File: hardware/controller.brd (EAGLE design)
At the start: 44.5 x 33 mm, 27 parts, among them IC3 TS5205, J1 PIN2F061.100, J2 PIN2F061.100, J3 PIN2F061.100, K1 G5LE, K2 G5LE, Q1 ABM8G, Q2 BC846ASMD, Q3 BC846ASMD, X1 FCI-USB-MICRO-B

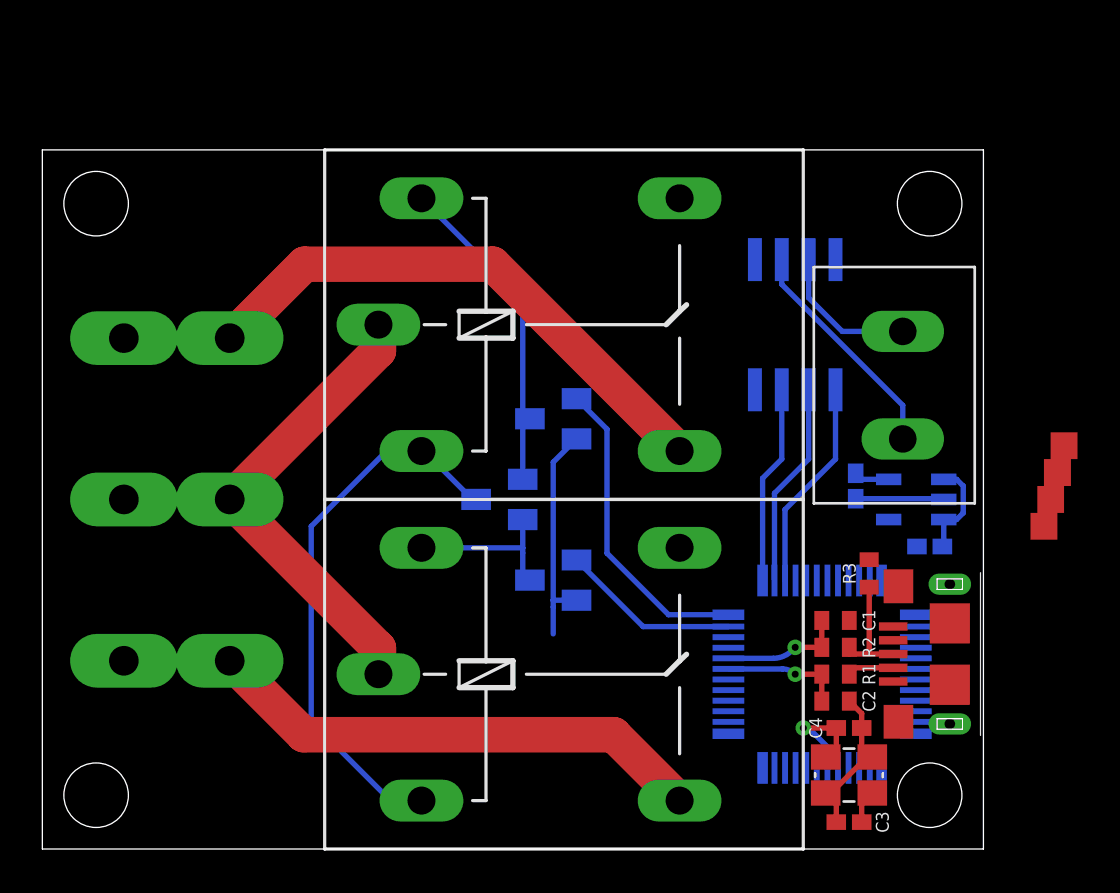
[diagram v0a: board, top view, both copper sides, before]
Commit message: hardware: first attempt with triacs
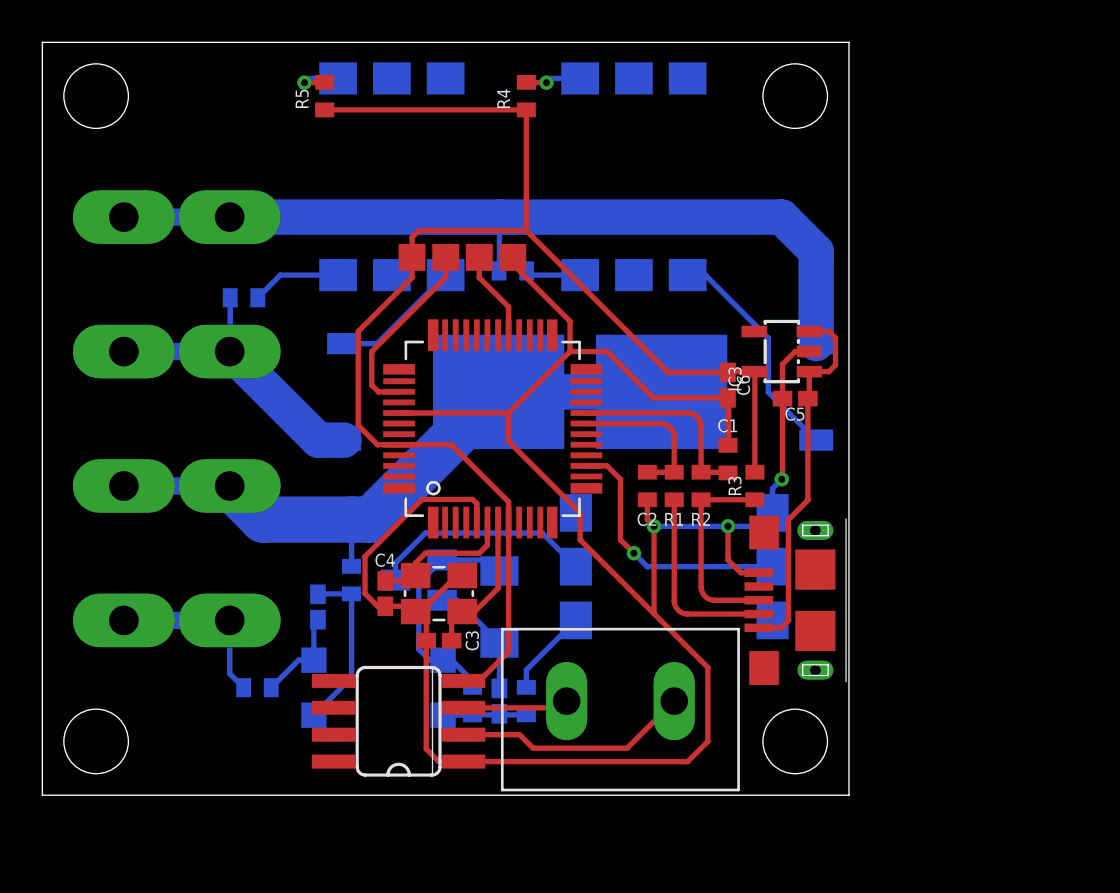
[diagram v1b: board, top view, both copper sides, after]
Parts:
- removed D3: BAT54C, diode:SOT23
- removed K1, K2: G5LE, relay:G5LE
- removed Q3: BC846ASMD, transistor-npn:SOT23
- added B1: MB6S, rectifier:SOIC-4
- added C7, C8: 1nF, resistor:C0402K
- added D1: (no value), diode:SOD80C
- added J4: PIN2F061.100, con-faston:F061.100
- added OK1: 4N35SM, optocoupler:DIL6-SMD
- added R10: 44kΩ, resistor:R0402
- added R11: 1kΩ, resistor:R0402
- added R4, R5, R6, R7: 33Ω, resistor:R0402
- added R8, R9: 440kΩ, resistor:R0402
- added U$4, U$5: MOC3063, crawford:SMD6
- added U$6, U$7: BT137S-600D, crawford:TO-252
- Q2: value BC846ASMD -> BC817-40SMD; device transistor-npn:SOT23 -> transistor-npn:SOT23-BEC
- moved TP6 32.1 mm to (17.5, 27.9)
- moved TP1 31.0 mm to (19.1, 27.9)
- moved TP2 29.3 mm to (20.6, 27.9)
- moved TP7 27.7 mm to (22.2, 27.9)
- moved U$2 26.5 mm to (16.8, 6.03), flipped to the top, turned to 90 degrees
- moved C4 22.8 mm to (16.2, 12.1), turned to 270 degrees
- moved C3 21.2 mm to (18.7, 9.84)
- moved Q1 21.2 mm to (18.7, 12.1)
- moved J1 21.0 mm to (6.35, 29.8)
- moved U$3 20.0 mm to (27.3, 6.99), turned to 270 degrees
- moved U$1 19.4 mm to (21.3, 19.8), flipped to the top
- moved C2 13.5 mm to (28.6, 17.1), turned to 270 degrees
- moved J3 13.3 mm to (6.35, 10.8)
- moved R1 11.7 mm to (29.8, 17.1), turned to 270 degrees
- moved R2 9.92 mm to (31.1, 17.1), turned to 270 degrees
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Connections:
- removed net B_K1: Q3.1, U$1.23
- removed net B_K2: Q2.1, U$1.24
- new net INT_ZX: OK1.5, U$1.15
- new net N$12: J1.A1, J1.A2, R6.2, U$6.1
- new net N$13: U$4.4, U$6.2
- new net N$14: U$5.4, U$7.2
- new net N$15: B1.-, C8.1, R10.1, R11.1
- new net N$16: B1.+, D1.C, Q2.B, R10.2
- new net N$17: B1.~1, C7.1, R9.2
- new net N$18: B1.~2, C7.2, R8.2
- new net N$19: OK1.1, R11.2
- new net N$20: OK1.2, Q2.C
- new net N$21: C8.2, D1.A, Q2.E
- new net N$23: U$4.2
- new net N$24: U$5.2
- new net V+: J3.A1, J3.A2, R8.1
- new net V-: J4.A1, J4.A2, R9.1, U$6.3, U$7.3
- net +3V3: now also R4.1, R5.1; no longer D3.3, K1.1, K2.1
- net CS: no longer U$1.26
- net GND: now also OK1.4; no longer Q2.2, Q3.2
- net N$1: now also R6.1, U$4.6; no longer J2.A1, J2.A2, K1.P, K2.P
- net N$10: now also R4.2, U$4.1; no longer D3.2, K1.2, Q3.3
- net N$11: now also R5.2, U$5.1; no longer D3.1, K2.2, Q2.3
- net N$2: now also J2.A1, J2.A2, R7.2, U$7.1; no longer J3.A1, J3.A2, K2.S
- net N$8: now also R7.1, U$5.6; no longer J1.A1, J1.A2, K1.S
- net SCK: no longer U$1.27
- net SO: no longer U$1.25
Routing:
- net GND: track 22.7 -> 103.7 mm, vias 0 -> 3
- net N$12: track 0.00 -> 40.3 mm
- net +3V3: track 28.0 -> 67.4 mm
- net V-: track 0.00 -> 30.8 mm
- net N$8: track 24.0 -> 4.24 mm
- net N$1: track 22.3 -> 2.61 mm
- net B_K2: track 14.8 -> 0.00 mm
- net +5V: track 4.71 -> 17.9 mm
- net N$11: track 15.6 -> 2.63 mm, vias 0 -> 1
- net INT_ZX: track 0.00 -> 12.4 mm, vias 0 -> 1
- net N$2: track 26.4 -> 14.7 mm
- net N$16: track 0.00 -> 11.1 mm
- net N$13: track 0.00 -> 10.8 mm
- net N$20: track 0.00 -> 10.6 mm
- net SCK: track 10.00 -> 0.00 mm
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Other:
- board size 44.5 x 33 mm -> 38.1 x 35.6 mm
- board text added: "HOT"
- board text added: "NEUTRAL"
- board text removed: "VAC"
